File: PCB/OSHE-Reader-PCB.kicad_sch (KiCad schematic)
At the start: 33 parts, among them Q1 Si1308EDL

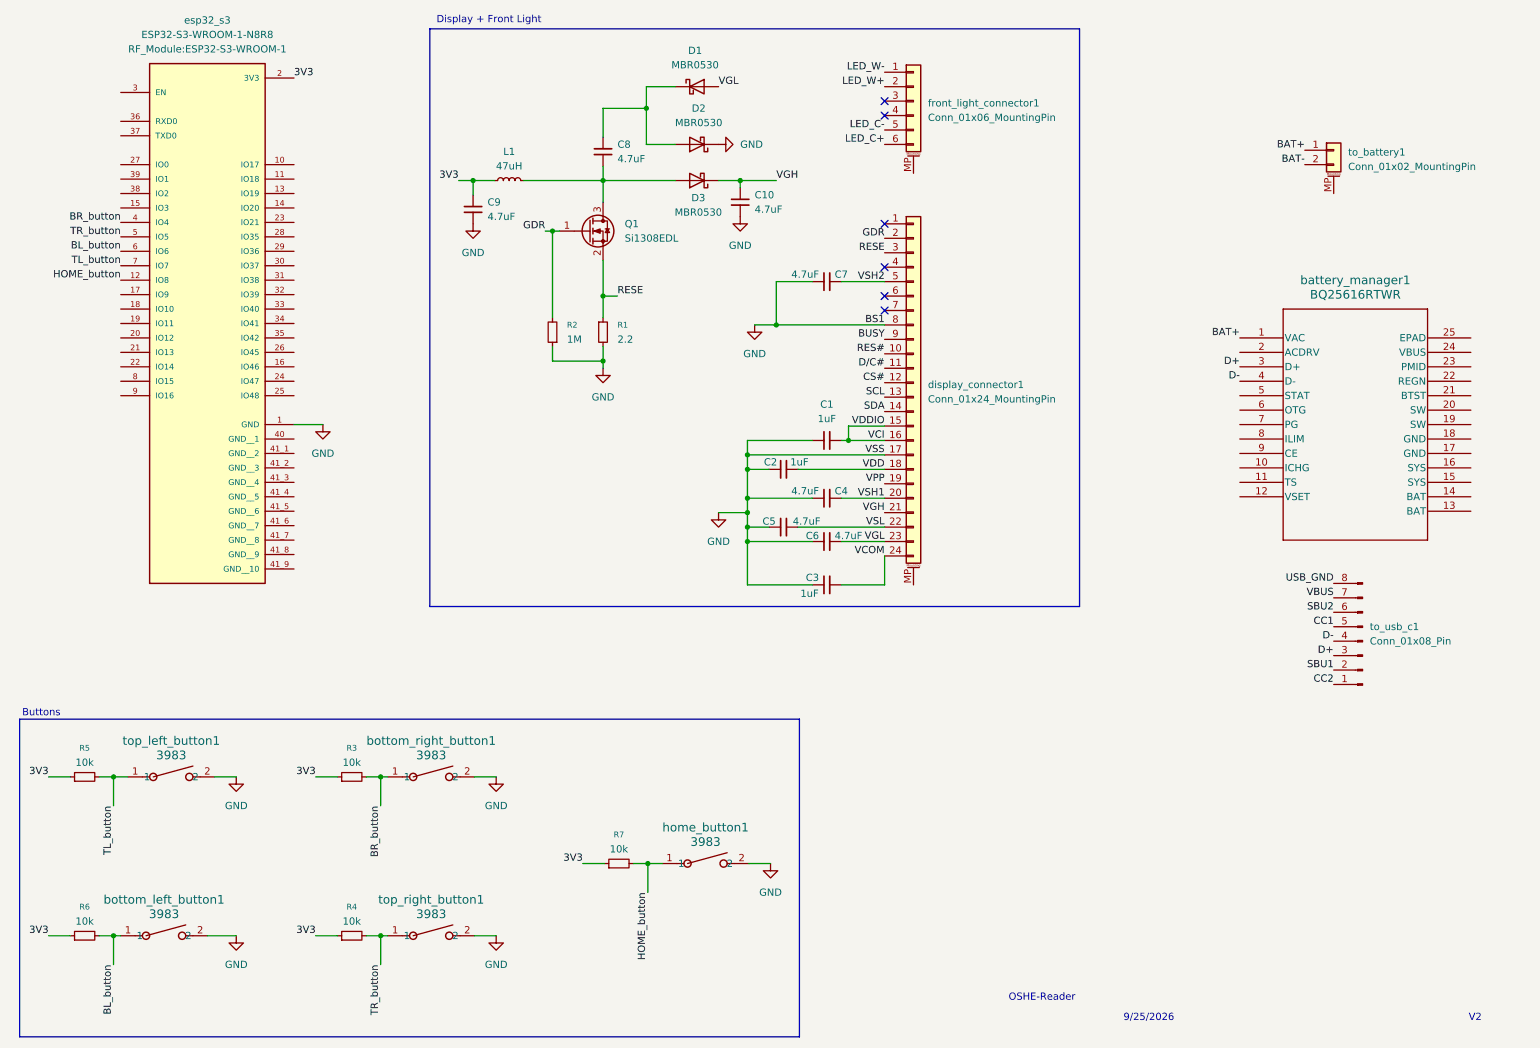
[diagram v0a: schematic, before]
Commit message: Updated battery charger + tidied up
- made hierarchical sheets + pins for cleaner look
- battery charger is wired up
- usb c port is wired up
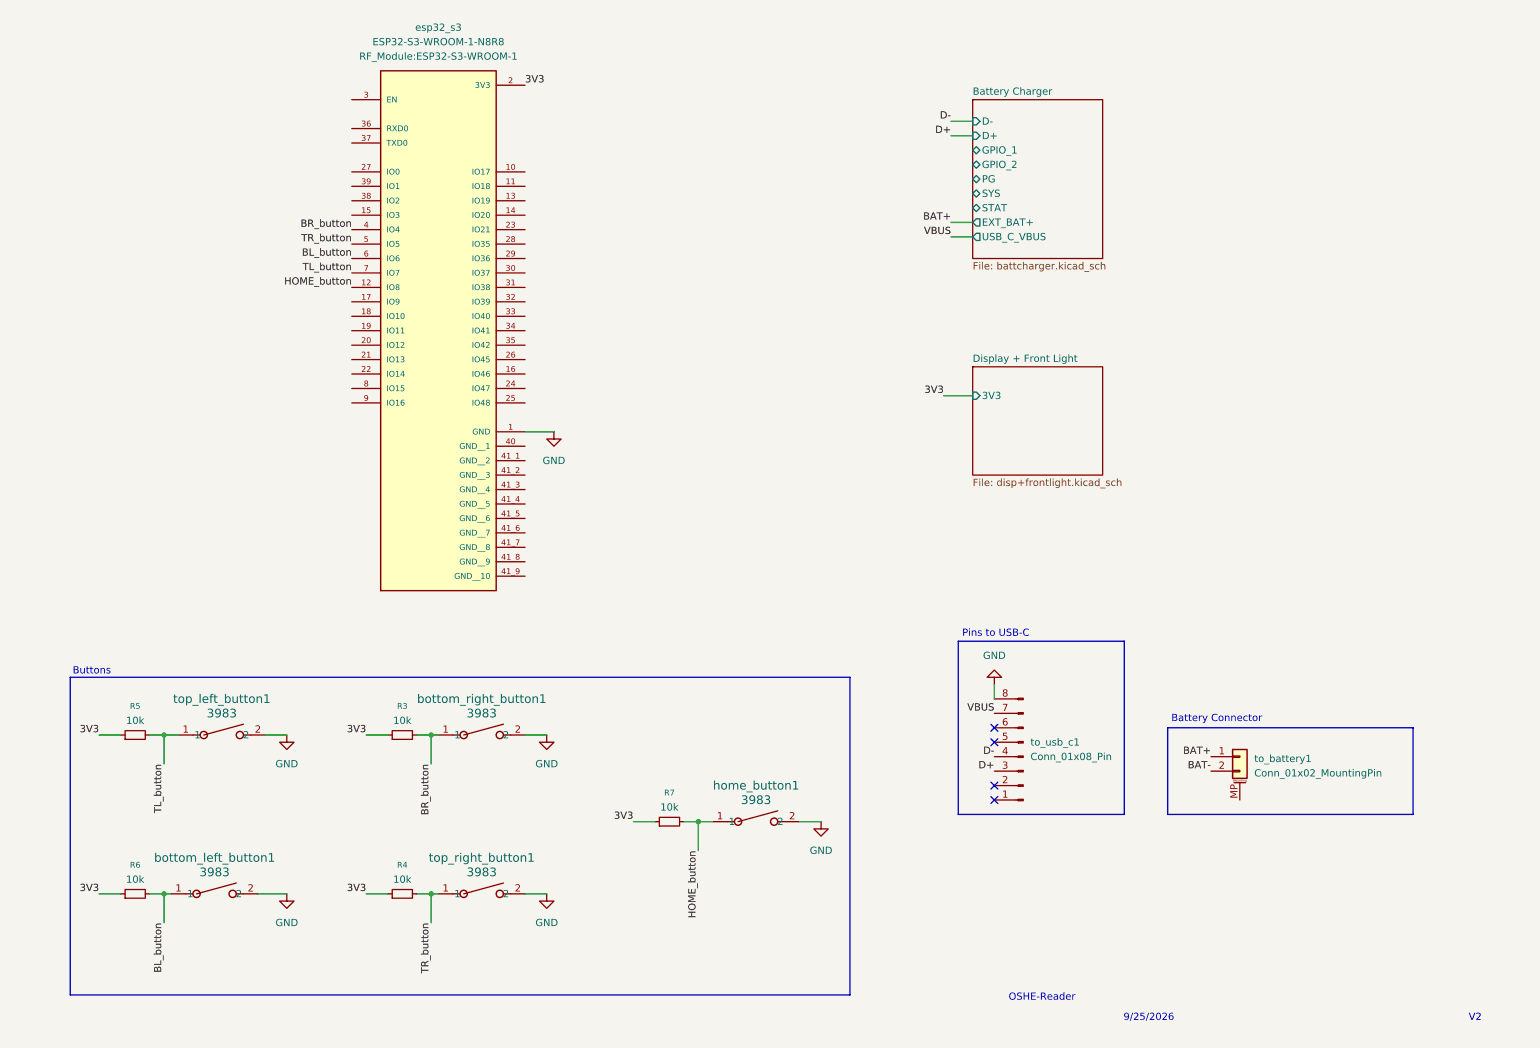
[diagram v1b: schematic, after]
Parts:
- removed C1, C2, C3: 1uF, Capacitor_SMD:C_1206_3216Metric_Pad1.33x1.80mm_HandSolder, symbol Device:C_Small
- removed C10, C8, C9: 4.7uF, Package_TO_SOT_SMD:SOT-23-6, symbol Device:C_Small
- removed C4, C5, C6, C7: 4.7uF, Capacitor_SMD:C_1206_3216Metric_Pad1.33x1.80mm_HandSolder, symbol Device:C_Small
- removed D1, D2, D3: MBR0530, Diode_SMD:D_SOD-123, symbol Diode:MBR0530
- removed L1: 47uH, Package_SO:SOIC-20W_7.5x12.8mm_P1.27mm, symbol Device:L_Small
- removed Q1: Si1308EDL, Package_TO_SOT_SMD:SOT-323_SC-70, symbol Transistor_FET:Si1308EDL
- removed R1: 2.2, Package_TO_SOT_SMD:SOT-323_SC-70, symbol Device:R_Small
- removed R2: 1M, symbol Device:R_Small
- removed battery_manager1: BQ25616RTWR, BQ25616RTWR:QFN24_RTW_TEX, symbol BQ25616RTWR:BQ25616RTWR
- removed display_connector1: Conn_01x24_MountingPin, Connector_FFC-FPC:Hirose_FH12-24S-0.5SH_1x24-1MP_P0.50mm_Horizontal, symbol Connector_Generic_MountingPin:Conn_01x24_MountingPin
- removed front_light_connector1: Conn_01x06_MountingPin, Connector_FFC-FPC:Hirose_FH12-6S-0.5SH_1x06-1MP_P0.50mm_Horizontal, symbol Connector_Generic_MountingPin:Conn_01x06_MountingPin
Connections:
- net USB_GND is gone; now on net GND: to_usb_c1.8 (Pin_8)
- net CC1: no longer names the net of to_usb_c1.5 (Pin_5)
- net CC2: no longer names the net of to_usb_c1.1 (Pin_1)
- net SBU1: no longer names the net of to_usb_c1.2 (Pin_2)
- net SBU2: no longer names the net of to_usb_c1.6 (Pin_6)
- no-connect marks 6 -> 4
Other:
- added sheet Battery Charger (battcharger.kicad_sch)
- added sheet Display + Front Light (disp+frontlight.kicad_sch)
- note added: "Battery Connector"
- note added: "Pins to USB-C"
- note removed: "Display + Front Light"
- moved on the sheet: R3, R4, R5, R6, R7, bottom_left_button1, bottom_right_button1, esp32_s3, home_button1, to_battery1, to_usb_c1, top_left_button1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

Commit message: Finished schematic
added ldo reg for system power from battery charger ic
finished up all wiring
footprints added
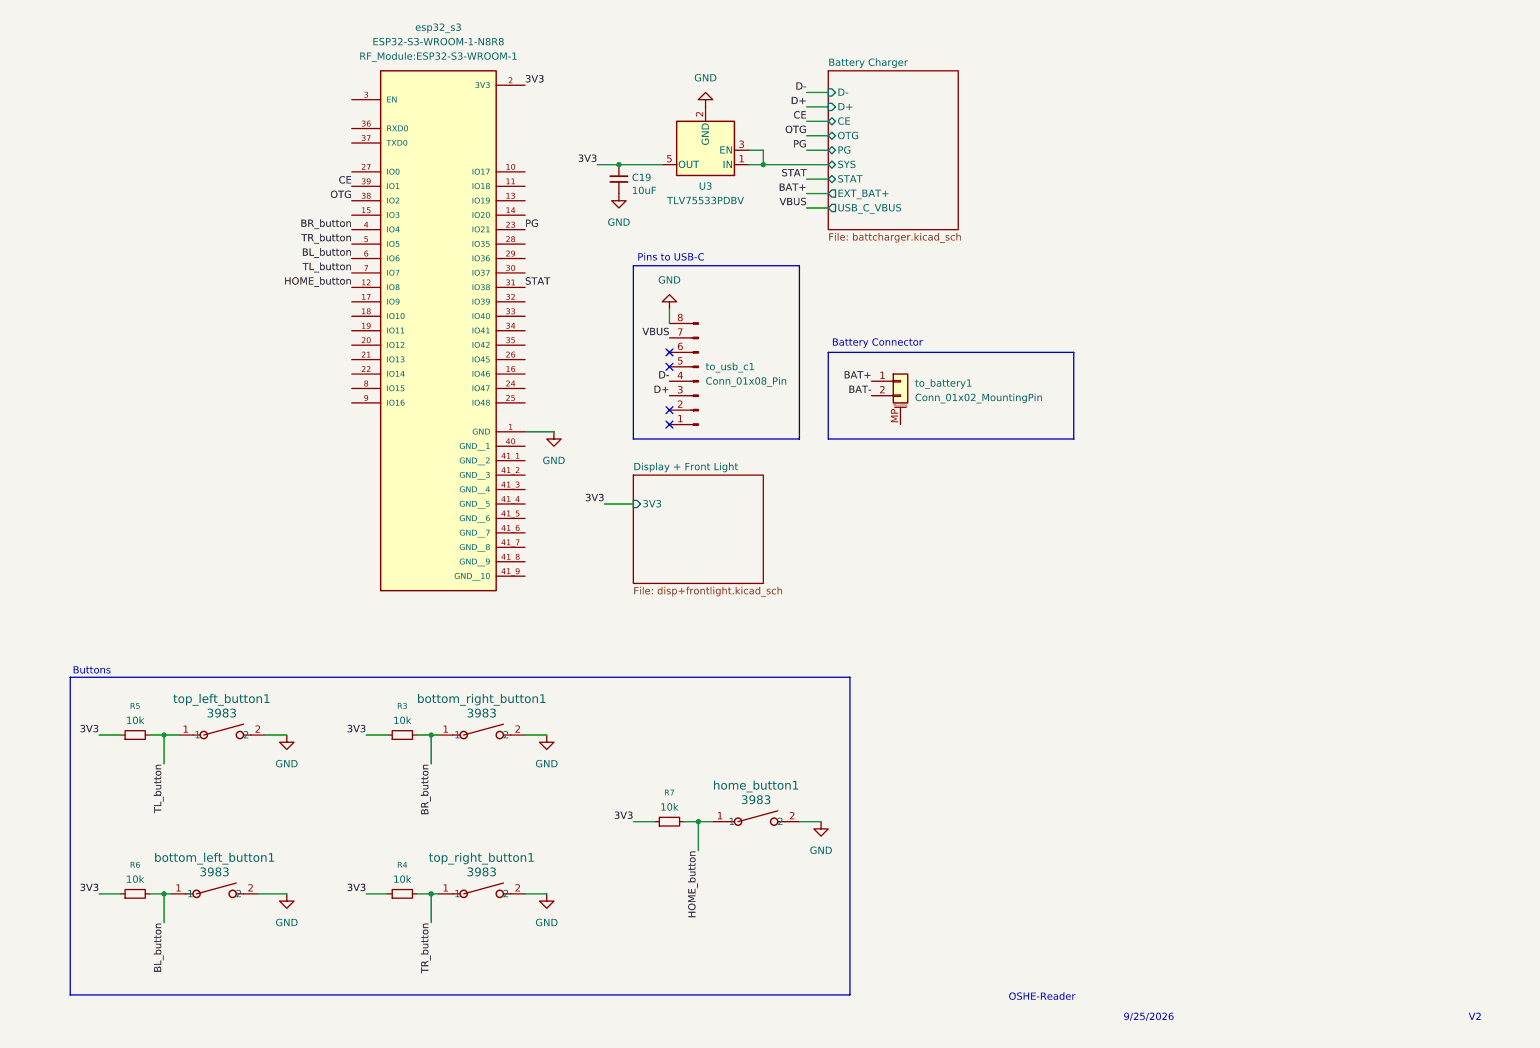
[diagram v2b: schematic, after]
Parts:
- added C19: 10uF, Capacitor_SMD:C_1206_3216Metric_Pad1.33x1.80mm_HandSolder, symbol Device:C_Small
- added U3: TLV75533PDBV, Package_TO_SOT_SMD:SOT-23-5, symbol Regulator_Linear:TLV75533PDBV
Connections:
- net 3V3: now also C19.1, U3.5 (OUT)
- net Battery Charger/SYS: now also U3.1 (IN), U3.3 (EN)
- net GND: now also C19.2, U3.2 (GND)
- net PG: now reaches esp32_s3.23 (IO21)
- net STAT: now reaches esp32_s3.31 (IO38)
- net OTG: now reaches esp32_s3.38 (IO2)
- net CE: now reaches esp32_s3.39 (IO1)
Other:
- sheet Battery Charger ports: added CE, OTG; removed GPIO_1, GPIO_2
- moved on the sheet: to_battery1, to_usb_c1

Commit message: PCB Time
Started routing the PCB
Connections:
- net BL_button: now also esp32_s3.7 (IO7); no longer esp32_s3.6 (IO6)
- net TL_button: now also esp32_s3.6 (IO6); no longer esp32_s3.7 (IO7)
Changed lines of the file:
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@@
 		)
 	)
-	(label "BL_button"
+	(label "TL_button"
 		(at 72.39 59.69 180)
 		(effects
@@
 		)
 	)
-	(label "TL_button"
+	(label "BL_button"
 		(at 72.39 62.23 180)
 		(effects

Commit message: Rechecked schematic + started PCB
Schematic:
+ routed screen connector
+ fixed charger to 500mA and routed data to MCU
+ added micro sd card reader
+ added uart, jtag, and boot selector pins
= changed esp32 symbol
= made 3v3 a power symbol (idk why i didnt do this from the start)

TODO:
pick resistor values for thermistor
put all passives on pcb
route pcb
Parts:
- removed esp32_s3: ESP32-S3-WROOM-1-N8R8, RF_Module:ESP32-S3-WROOM-1, symbol ESP32-S3-WROOM-1-N8R8:ESP32-S3-WROOM-1-N8R8
- added C22: 1uF, Inductor_SMD:L_1206_3216Metric_Pad1.22x1.90mm_HandSolder, symbol Device:C_Small
- added C25: 0.1uF, Capacitor_SMD:C_1206_3216Metric, symbol Device:C
- added C26: 10uF, Capacitor_SMD:C_1206_3216Metric, symbol Device:C
- added J1: UART, Connector_PinHeader_2.54mm:PinHeader_1x04_P2.54mm_Vertical, symbol Connector:Conn_01x04_Pin
- added J2: 112L-TDA0, 112L-TDA0:CONN_112L-TDA0_ATT, symbol 112L_TDA0:112L-TDA0
- added J3: JTAG, Connector_PinHeader_2.54mm:PinHeader_1x04_P2.54mm_Vertical, symbol Connector:Conn_01x04_Pin
- added J5: boot_select, Connector_PinHeader_2.54mm:PinHeader_1x02_P2.54mm_Vertical, symbol Connector:Conn_01x02_Pin
- added R21: 10k, Resistor_SMD:R_1206_3216Metric_Pad1.30x1.75mm_HandSolder, symbol Device:R_Small
- added U4: ESP32-S3-WROOM-1, RF_Module:ESP32-S3-WROOM-1, symbol RF_Module:ESP32-S3-WROOM-1
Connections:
- net BL_button: now also U4.7 (IO7)
- net BR_button: now also U4.4 (IO4)
- net CE: now also U4.39 (IO1)
- net D+: now also U4.14 (USB_D+)
- net D-: now also U4.13 (USB_D-)
- net GND: now also C22.2, C25.2, C26.2, J1.4 (Pin_4), J2.19 (GND), J2.20 (GND), J2.21 (GND), J2.22 (GND), J2.23 (GND), J2.6 (VSS), J5.2 (Pin_2), U4.1 (GND), U4.40 (GND), U4.41 (GND)
- net HOME_button: now also U4.12 (IO8)
- net OTG: now also U4.38 (IO2)
- net PG: now also U4.23 (IO21)
- net STAT: now also U4.31 (IO38)
- net TL_button: now also U4.6 (IO6)
- net TR_button: now also U4.5 (IO5)
- net 3V3 renamed +3V3
- net +3V3: now also C25.1, C26.1, J1.1 (Pin_1), J2.4 (VDD), R21.1, U4.2 (3V3)
- new net: J5.1 (Pin_1), U4.27 (IO0)
- new net: C22.1, R21.2, U4.3 (EN)
- new net BUSY: U4.24 (IO47)
- new net CIPO: J2.7 (DAT0), U4.21 (IO13)
- new net COPI: J2.3 (CMD), U4.19 (IO11)
- new net D/C: U4.17 (IO9)
- new net EPAP_CS: U4.18 (IO10)
- new net RES_SCR: U4.25 (IO48)
- new net RX: J1.3 (Pin_3), U4.36 (RXD0)
- new net SCL: J2.5 (CLK), U4.20 (IO12)
- new net SD_CS: J2.2 (CD/DAT3), U4.22 (IO14)
- new net TCK: J3.4 (Pin_4), U4.32 (IO39)
- new net TDI: J3.2 (Pin_2), U4.34 (IO41)
- new net TDO: J3.3 (Pin_3), U4.33 (IO40)
- new net TMS: J3.1 (Pin_1), U4.35 (IO42)
- new net TX: J1.2 (Pin_2), U4.37 (TXD0)
- no-connect marks 4 -> 27
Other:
- sheet Battery Charger ports: added none; removed D+, D-
- sheet Display + Front Light ports: added BUSY, CS#, D/C#, RES#, SCL, SDA; removed 3V3
- note added: "JTAG Debugger"
- note added: "Jump me to select boot mode!"
- note added: "SD Card Reader"
- note added: "UART Debugger"
- moved on the sheet: to_usb_c1

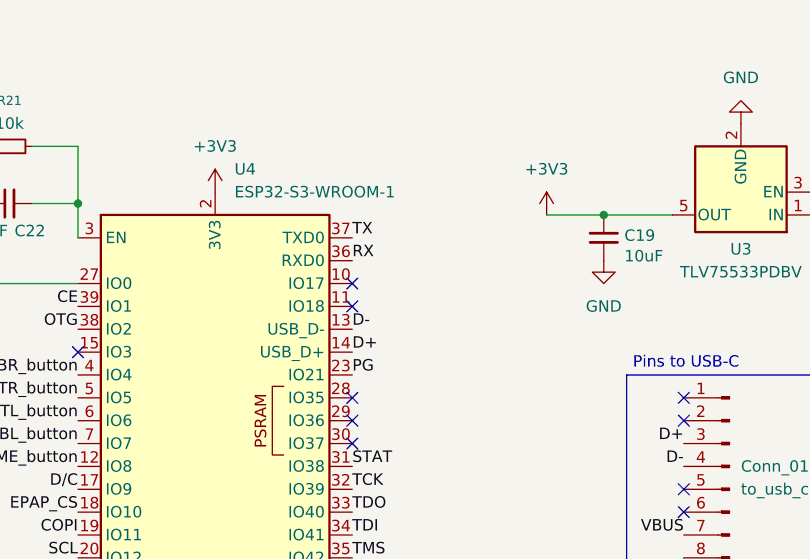
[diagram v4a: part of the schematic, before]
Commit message: Started Rerouting Board
-Got a gnd plane
-got all components re-organized
-maybe need a 3.3v plane???
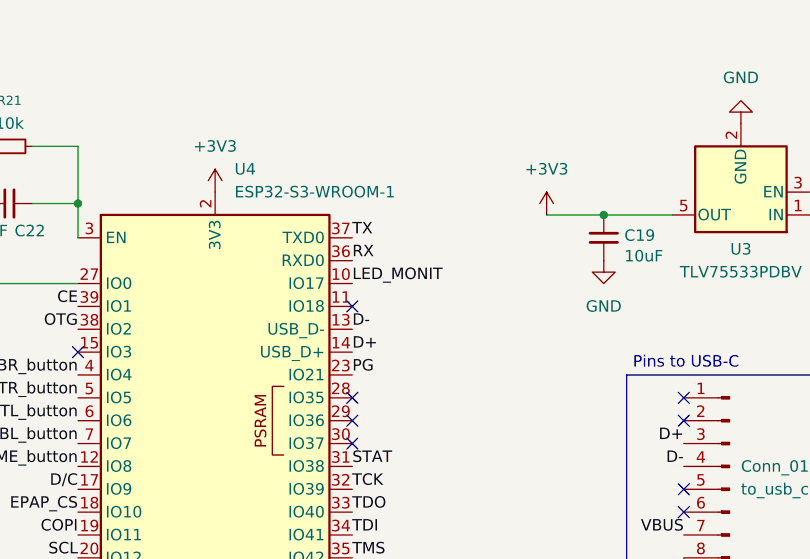
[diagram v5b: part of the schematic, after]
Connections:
- net LED_MONIT: now reaches U4.10 (IO17)
- no-connect marks 27 -> 26
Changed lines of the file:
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@@
+	)
+	(no_connect
+		(at 60.96 58.42)
 	)
 	(no_connect
@@
 	)
 	(no_connect
-		(at 60.96 58.42)
-	)
-	(no_connect
 		(at 91.44 66.04)
 	)
 	(no_connect
 		(at 247.65 128.27)
-	)
-	(no_connect
-		(at 91.44 50.8)
 	)
 	(no_connect
@@
 		(effects
 			(font
+				(size 1.27 1.27)
+			)
+			(justify left bottom)
+		)
+	)
+	(label "LED_MONIT"
+		(at 91.44 50.8 0)
+		(effects
+			(font
